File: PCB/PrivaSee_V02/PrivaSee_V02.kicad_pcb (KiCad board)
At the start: 4 copper layers, 73.8 x 90 mm, 32 parts, among them J1 RFPC-SMA27-F, J2 Batt_Solder_Point, J3 Conn_02x06_Odd_Even, J4 VOUT_TEST, J5 GND_TEST, J6 IR_TEST, J7 RF_TEST, SW1 Switch, SW2 SW_Push, U2 LM358, U3 254, U4 DFR0568, U6 ESP32-C5-DevKitC-1

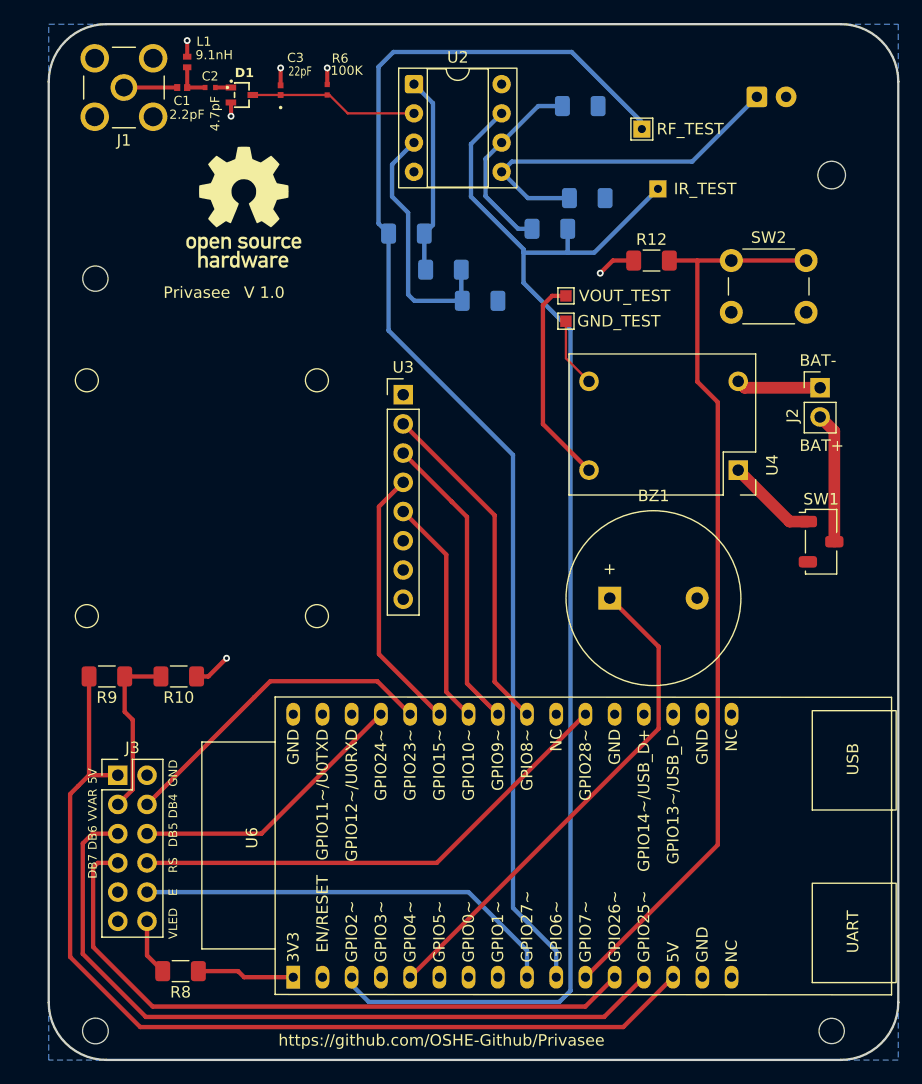
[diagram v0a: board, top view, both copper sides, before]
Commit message: Schematic + RF Fixes
Also changed button position
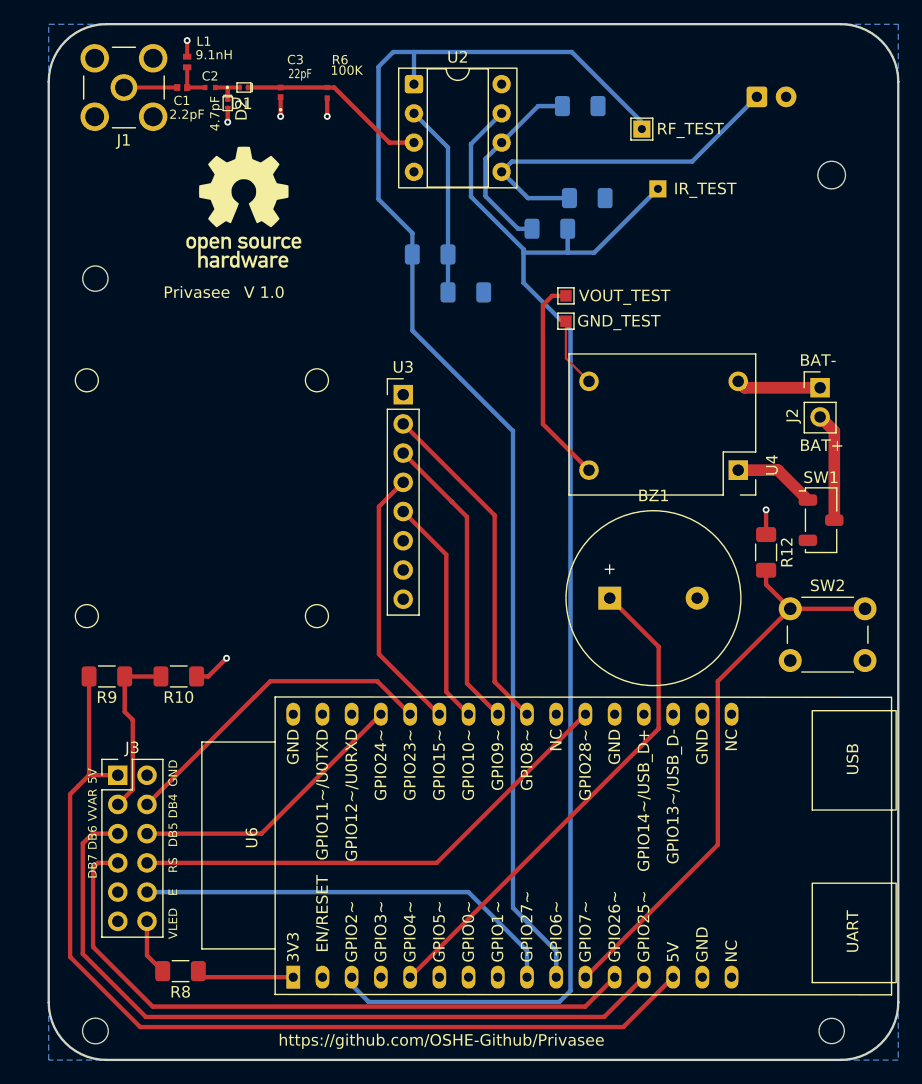
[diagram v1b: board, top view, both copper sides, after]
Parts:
- removed R2: 470 Ohm, Resistor_SMD:R_1206_3216Metric_Pad1.30x1.75mm_HandSolder
- added D2: BAT_15-02EL_E6327, JLCImport:BAT_15-02EL_E6327, F.Cu at (81.6, 28.5)
- D1: value BAT1504WH6327XTSA1 -> BAT_15-02EL_E6327; footprint JLCImport:BAT1504WH6327XTSA1 -> JLCImport:BAT_15-02EL_E6327
- moved SW2 30.7 mm to (130.5, 72.4)
- moved R12 27.3 mm to (128.4, 67.5), turned to -90 degrees
- moved SW1 1.87 mm to (133.2, 64.7)
- moved R1 1.76 mm to (99.2, 41.6), turned to 0 degrees
- moved R7 1.44 mm to (102.3, 44.9)
- moved D1 0.67 mm to (83.0, 27.1)
- moved R6 0.26 mm to (90.2, 27.5)
- moved C3 0.19 mm to (86.2, 27.5)
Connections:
- C3 pad 1: Net-(D1-C/A) -> GND
- C3 pad 2: GND -> Net-(D1-C)
- D1 pad 1: Net-(D1-A) -> Net-(D1-C)
- D1 pad 2: GND -> Net-(D1-A)
- R1 pad 1: Net-(U2A-+) -> Net-(J7-Pin_1)
- R1 pad 2: Net-(R1-Pad2) -> Net-(U2A--)
- R6 pad 1: GND -> Net-(D1-C)
- R6 pad 2: Net-(D1-C/A) -> GND
- R7 pad 1: Net-(U2A-+) -> Net-(U2A--)
- U2 pad 1: Net-(R1-Pad2) -> Net-(J7-Pin_1)
- U2 pad 2: Net-(D1-C/A) -> Net-(U2A--)
- U2 pad 3: Net-(U2A-+) -> Net-(D1-C)
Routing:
- net Net-(U6-GPIO7): track 79.7 -> 50.1 mm
- net Net-(U2A-+): track 22.1 -> 0.00 mm
- net Net-(R1-Pad2): track 17.2 -> 0.00 mm
- net Net-(U2A--): track 0.00 -> 17.1 mm
- net Net-(D1-C): track 0.00 -> 16.4 mm
- net Net-(D1-C/A): track 15.0 -> 0.00 mm
- net Net-(J7-Pin_1): track 112.5 -> 115.3 mm
- net Net-(D1-A): track 1.35 -> 3.22 mm
- net /BAT+: track 11.4 -> 9.48 mm
- net GND: track 18.3 -> 17.5 mm
- net Net-(SW1-C): track 7.91 -> 7.13 mm
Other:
- board text removed: "D1"

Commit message: potentiometer addition
Included a pot for variable gain instead of set amount
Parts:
- added R11: 3310Y-001-103L, Snapeda:TRIM_3310Y-001-103L, F.Cu at (104.5, 52.7)
- R1: value 200 -> 100
- R7: value 10 -> 100
- moved ? 6.00 mm to (77.0, 37.5)
- moved R7 2.20 mm to (103.4, 43.0)
- moved R1 1.70 mm to (99.2, 39.9)
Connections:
- R1 pad 1: Net-(J7-Pin_1) -> Net-(R1-Pad1)
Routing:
- net Net-(R1-Pad1): track 0.00 -> 15.4 mm
- net Net-(U2A--): track 17.1 -> 15.7 mm
- net Net-(J7-Pin_1): track 115.3 -> 116.0 mm

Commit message: trace changes
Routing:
- net GND: track 17.5 -> 15.0 mm
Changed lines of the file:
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@@
 		(start 80.527284 27.0882)
 		(end 81.6 27.0882)
-		(width 0.355476)
+		(width 0.5)
 		(layer "F.Cu")
 		(net "Net-(D1-A)")
@@
 		(start 81.6 28.17)
 		(end 81.6 27.0882)
-		(width 0.381)
+		(width 0.5)
 		(layer "F.Cu")
 		(net "Net-(D1-A)")
@@
 		(start 81.6 27.0882)
 		(end 82.67 27.0882)
-		(width 0.355476)
+		(width 0.5)
 		(layer "F.Cu")
 		(net "Net-(D1-A)")
 	)
 	(segment
-		(start 78.075 27.0882)
-		(end 78.075 25.33)
-		(width 0.355476)
+		(start 78.075 25.33)
+		(end 78.075 27.0882)
+		(width 0.5)
 		(layer "F.Cu")
 		(net "Net-(C1-Pad1)")
 	)
 	(segment
-		(start 78.075 27.0882)
-		(end 79.638284 27.0882)
-		(width 0.355476)
+		(start 79.638284 27.0882)
+		(end 78.075 27.0882)
+		(width 0.5)
 		(layer "F.Cu")
 		(net "Net-(C1-Pad1)")
@@
 	)
 	(segment
-		(start 90.25 29.6)
-		(end 90.25 28.0026)
-		(width 0.381)
+		(start 78.075 23.6)
+		(end 78.075 24.41)
+		(width 0.5)
 		(layer "F.Cu")
 		(net "GND")
@@
 	)
 	(segment
+		(start 81.6 29.6)
+		(end 81.6 28.845)
+		(width 0.45)
+		(layer "F.Cu")
+		(net "GND")
+	)
+	(segment
 		(start 78.08 24.4)
 		(end 78.07 24.41)
 		(width 0.2)
+		(layer "F.Cu")
+		(net "GND")
+	)
+	(segment
+		(start 90.25 28.9)
+		(end 90.25 28.0026)
+		(width 0.381)
+		(layer "F.Cu")
+		(net "GND")
+	)
+	(segment
+		(start 86.2 28.9)
+		(end 86.2 27.9264)
+		(width 0.381)
 		(layer "F.Cu")
 		(net "GND")
@@
 		(net "GND")
 	)
-	(segment
-		(start 81.6 30.1)
-		(end 81.6 28.83)
-		(width 0.381)
-		(layer "F.Cu")
-		(net "GND")
-	)
-	(segment
-		(start 86.2 29.6)
-		(end 86.2 27.9264)
-		(width 0.381)
-		(layer "F.Cu")
-		(net "GND")
-	)
-	(segment
-		(start 78.075 23.01)
-		(end 78.075 24.4)
-		(width 0.355476)
-		(layer "F.Cu")
-		(net "GND")
-	)
 	(via
-		(at 81.6 30.1)
+		(at 81.6 29.6)
 		(size 0.6)
 		(drill 0.3)
@@
 	)
 	(via
-		(at 90.25 29.6)
+		(at 90.25 28.9)
 		(size 0.6)
 		(drill 0.3)
@@
 	)
 	(via
-		(at 86.2 29.6)
+		(at 86.2 28.9)
 		(size 0.6)
 		(drill 0.3)
@@
 	)
 	(via
-		(at 78.075 23.01)
+		(at 78.075 23.6)
 		(size 0.6)
 		(drill 0.3)

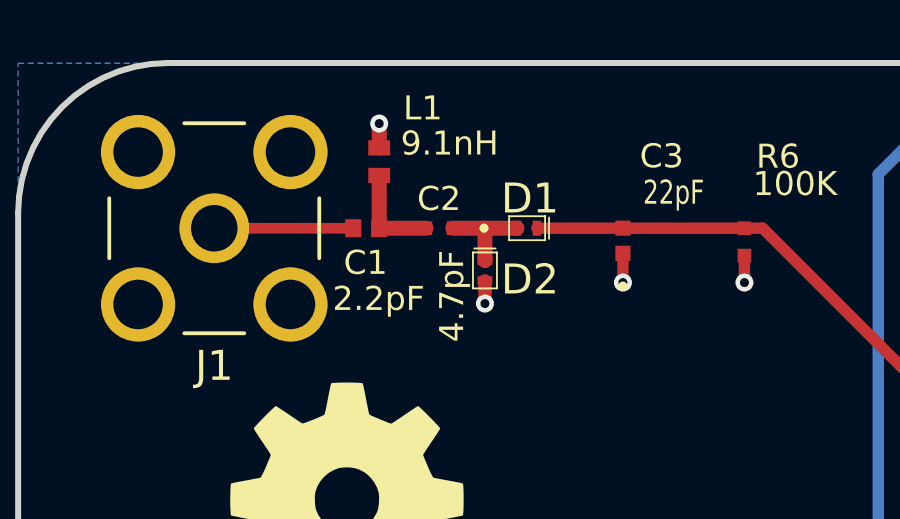
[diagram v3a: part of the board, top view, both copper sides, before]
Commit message: trace adjustments
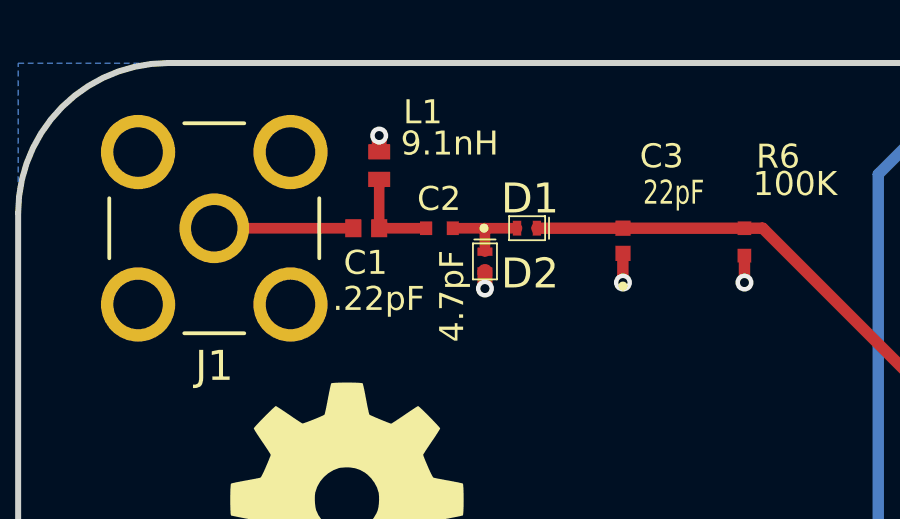
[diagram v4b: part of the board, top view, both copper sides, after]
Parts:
- moved D2 0.30 mm to (81.6, 28.2)
- moved L1 0.13 mm to (78.1, 25.0)
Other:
- board text added: ".22pF"
- board text removed: "2.2pF"
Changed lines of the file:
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@@
 	(footprint "Snapeda:INDC1006X60N"
 		(layer "F.Cu")
-		(at 78.075 24.87 -90)
+		(at 78.075 25 -90)
 		(property "Reference" "L1"
 			(at -1.78 -1.455 0)
@@
 	(footprint "JLCImport:BAT_15-02EL_E6327"
 		(layer "F.Cu")
-		(at 81.6 28.5 -90)
+		(at 81.6 28.2 -90)
 		(descr "1 Independent 110mA 350mV@10mA 4V 5uA@1V TSLP-2 Schottky Diodes ROHS")
 		(tags "BAT1502ELE6327 C533619 Infineon Technologies TSLP-2-19_L1.0-W0.6-P0.65-RD")
 		(property "Reference" "D2"
-			(at 0.3 -1.5 180)
+			(at 0.4 -1.5 180)
 			(layer "F.SilkS")
 			(effects
@@
 		)
 	)
-	(gr_text "2.2pF"
+	(gr_text ".22pF"
 		(at 76.52 29.91 0)
 		(layer "F.SilkS")
@@
 	)
 	(segment
-		(start 80.527284 27.0882)
+		(start 81.6 27.87)
 		(end 81.6 27.0882)
-		(width 0.5)
+		(width 0.355476)
 		(layer "F.Cu")
 		(net "Net-(D1-A)")
 	)
 	(segment
-		(start 81.6 28.17)
+		(start 80.527284 27.0882)
 		(end 81.6 27.0882)
-		(width 0.5)
+		(width 0.355476)
 		(layer "F.Cu")
 		(net "Net-(D1-A)")
@@
 		(start 81.6 27.0882)
 		(end 82.67 27.0882)
-		(width 0.5)
+		(width 0.355476)
 		(layer "F.Cu")
 		(net "Net-(D1-A)")
 	)
 	(segment
-		(start 78.075 25.33)
+		(start 78.075 25.46)
 		(end 78.075 27.0882)
-		(width 0.5)
+		(width 0.355476)
 		(layer "F.Cu")
 		(net "Net-(C1-Pad1)")
 	)
 	(segment
-		(start 79.638284 27.0882)
-		(end 78.075 27.0882)
-		(width 0.5)
+		(start 78.075 27.0882)
+		(end 79.638284 27.0882)
+		(width 0.355476)
 		(layer "F.Cu")
 		(net "Net-(C1-Pad1)")
@@
 	)
 	(segment
-		(start 78.075 23.6)
-		(end 78.075 24.41)
-		(width 0.5)
-		(layer "F.Cu")
-		(net "GND")
-	)
-	(segment
 		(start 111 50.625)
 		(end 111 47.3)
@@
 	)
 	(segment
+		(start 78.075 24)
+		(end 78.075 24.54)
+		(width 0.5)
+		(layer "F.Cu")
+		(net "GND")
+	)
+	(segment
 		(start 81.5 76.7)
 		(end 79.9172 78.2828)
@@
 	)
 	(segment
-		(start 81.6 29.6)
-		(end 81.6 28.845)
-		(width 0.45)
-		(layer "F.Cu")
-		(net "GND")
-	)
-	(segment
-		(start 78.08 24.4)
-		(end 78.07 24.41)
-		(width 0.2)
-		(layer "F.Cu")
-		(net "GND")
-	)
-	(segment
 		(start 90.25 28.9)
 		(end 90.25 28.0026)
@@
 		(net "GND")
 	)
+	(segment
+		(start 81.6 29.1)
+		(end 81.6 28.53)
+		(width 0.5)
+		(layer "F.Cu")
+		(net "GND")
+	)
 	(via
-		(at 81.6 29.6)
+		(at 81.6 29.1)
 		(size 0.6)
 		(drill 0.3)
@@
 	)
 	(via
-		(at 78.075 23.6)
+		(at 78.075 24)
 		(size 0.6)
 		(drill 0.3)

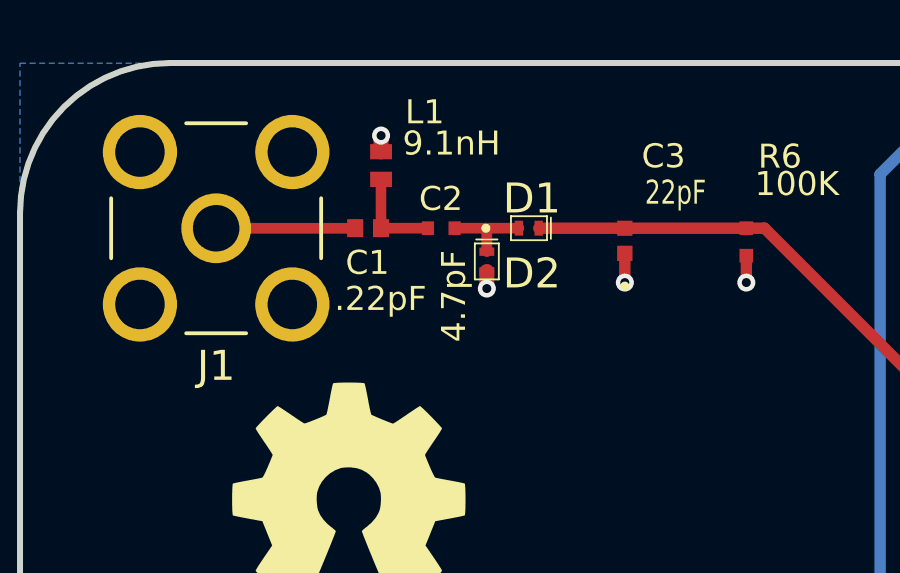
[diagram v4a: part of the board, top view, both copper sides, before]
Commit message: added taper to c2, d1, d2 junction
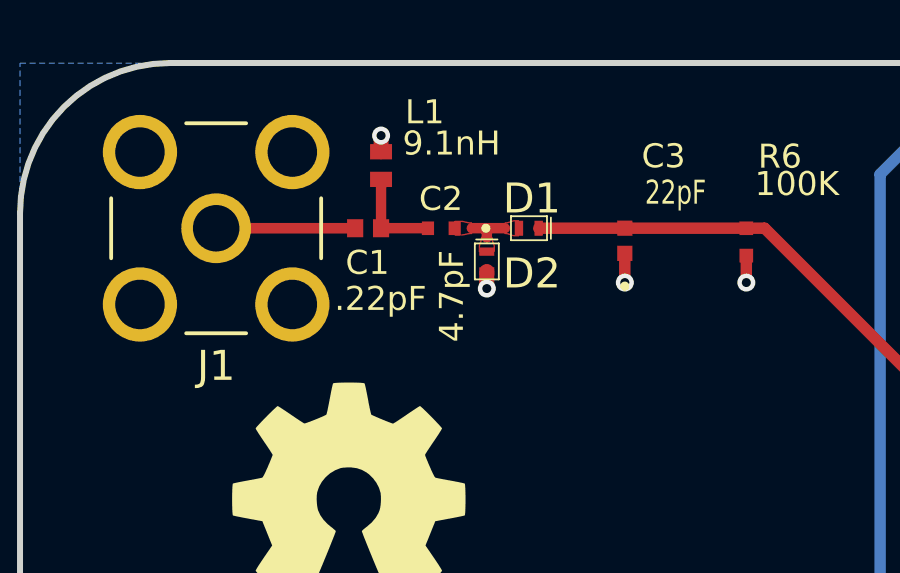
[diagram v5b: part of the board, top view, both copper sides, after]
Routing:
- net Net-(D1-A): track 2.92 -> 1.41 mm
- added copper zone on F.Cu, net Net-(D1-A)
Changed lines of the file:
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@@
 		)
 		(fp_text user "${REFERENCE}"
-			(at -0.107216 -1.8518 0)
+			(at 0 0 0)
 			(unlocked yes)
 			(layer "F.Fab")
@@
 	)
 	(gr_text "4.7pF"
-		(at 80.97 30.89 90)
+		(at 80.9 30.89 90)
 		(layer "F.SilkS")
 		(effects
@@
 	)
 	(segment
-		(start 81.6 27.87)
+		(start 81.6 27.4)
 		(end 81.6 27.0882)
-		(width 0.355476)
+		(width 0.35)
 		(layer "F.Cu")
 		(net "Net-(D1-A)")
 	)
 	(segment
-		(start 80.527284 27.0882)
+		(start 81.1 27.0882)
 		(end 81.6 27.0882)
-		(width 0.355476)
+		(width 0.35)
 		(layer "F.Cu")
 		(net "Net-(D1-A)")
@@
 	(segment
 		(start 81.6 27.0882)
-		(end 82.67 27.0882)
-		(width 0.355476)
+		(end 82.2 27.0882)
+		(width 0.35)
 		(layer "F.Cu")
 		(net "Net-(D1-A)")
 	)
 	(segment
-		(start 78.075 25.46)
-		(end 78.075 27.0882)
-		(width 0.355476)
+		(start 78.075 27.0882)
+		(end 78.075 25.46)
+		(width 0.35)
 		(layer "F.Cu")
 		(net "Net-(C1-Pad1)")
@@
 		(start 78.075 27.0882)
 		(end 79.638284 27.0882)
-		(width 0.355476)
+		(width 0.35)
 		(layer "F.Cu")
 		(net "Net-(C1-Pad1)")
@@
 	)
 	(zone
+		(net "Net-(D1-A)")
+		(layer "F.Cu")
+		(hatch edge 0.5)
+		(priority 17540)
+		(connect_pads yes
+			(clearance 0)
+		)
+		(min_thickness 0.0254)
+		(fill yes
+			(thermal_gap 0.5)
+			(thermal_bridge_width 0.5)
+			(island_removal_mode 0)
+		)
+		(polygon
+			(pts
+				(xy 81.6 27.37375) (xy 81.425 27.3972) (xy 81.4229 27.444513) (xy 81.4172 27.48503) (xy 81.408799 27.520128)
+				(xy 81.3986 27.551189) (xy 81.3875 27.579591) (xy 81.3764 27.606713) (xy 81.3662 27.633936) (xy 81.3578 27.662638)
+				(xy 81.3521 27.6942) (xy 81.35 27.73) (xy 81.35 27.87) (xy 81.6 27.9) (xy 81.85 27.87) (xy 81.85 27.73)
+				(xy 81.8479 27.6942) (xy 81.8422 27.662638) (xy 81.833799 27.633936) (xy 81.8236 27.606713) (xy 81.8125 27.579591)
+				(xy 81.8014 27.551189) (xy 81.7912 27.520128) (xy 81.7828 27.48503) (xy 81.7771 27.444513) (xy 81.775 27.3972)
+			)
+		)
+	)
+	(zone
+		(net "Net-(D1-A)")
+		(layer "F.Cu")
+		(hatch edge 0.5)
+		(priority 17540)
+		(connect_pads yes
+			(clearance 0)
+		)
+		(min_thickness 0.0254)
+		(fill yes
+			(thermal_gap 0.5)
+			(thermal_bridge_width 0.5)
+			(island_removal_mode 0)
+		)
+		(polygon
+			(pts
+				(xy 82.17375 27.0882) (xy 82.1972 27.2632) (xy 82.244513 27.2653) (xy 82.28503 27.271) (xy 82.320128 27.279399)
+				(xy 82.351189 27.2896) (xy 82.379591 27.3007) (xy 82.406713 27.3118) (xy 82.433936 27.321999) (xy 82.462638 27.3304)
+				(xy 82.4942 27.3361) (xy 82.53 27.3382) (xy 82.67 27.3382) (xy 82.7 27.0882) (xy 82.67 26.8382)
+				(xy 82.53 26.8382) (xy 82.4942 26.8403) (xy 82.462638 26.846) (xy 82.433936 26.854399) (xy 82.406713 26.8646)
+				(xy 82.379591 26.8757) (xy 82.351189 26.8868) (xy 82.320128 26.896999) (xy 82.28503 26.9054) (xy 82.244513 26.9111)
+				(xy 82.1972 26.9132)
+			)
+		)
+	)
+	(zone
+		(net "Net-(D1-A)")
+		(layer "F.Cu")
+		(hatch edge 0.5)
+		(priority 17540)
+		(connect_pads yes
+			(clearance 0)
+		)
+		(min_thickness 0.0254)
+		(fill yes
+			(thermal_gap 0.5)
+			(thermal_bridge_width 0.5)
+			(island_removal_mode 0)
+		)
+		(polygon
+			(pts
+				(xy 81.12625 27.0882) (xy 81.104064 26.9132) (xy 81.05157 26.911699) (xy 81.006336 26.907625) (xy 80.966901 26.901622)
+				(xy 80.931804 26.894332) (xy 80.899583 26.8864) (xy 80.868777 26.878467) (xy 80.837925 26.871177)
+				(xy 80.805567 26.865174) (xy 80.77024 26.8611) (xy 80.730484 26.8596) (xy 80.527284 26.8596) (xy 80.499852 27.0882)
+				(xy 80.527284 27.3168) (xy 80.730484 27.3168) (xy 80.77024 27.315299) (xy 80.805567 27.311225) (xy 80.837925 27.305222)
+				(xy 80.868777 27.297932) (xy 80.899583 27.29) (xy 80.931804 27.282067) (xy 80.966901 27.274777)
+				(xy 81.006336 27.268774) (xy 81.05157 27.2647) (xy 81.104064 27.2632)
+			)
+		)
+	)
+	(zone

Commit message: more trace changes
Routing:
- net Net-(D1-A): track 1.41 -> 2.88 mm
- removed copper zone on F.Cu, net Net-(D1-A)
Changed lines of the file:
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@@
 	)
 	(segment
-		(start 81.6 27.4)
+		(start 81.6 27.0882)
+		(end 82.67 27.0882)
+		(width 0.5)
+		(layer "F.Cu")
+		(net "Net-(D1-A)")
+	)
+	(segment
+		(start 81.6 27.0882)
+		(end 81.6 27.83)
+		(width 0.5)
+		(layer "F.Cu")
+		(net "Net-(D1-A)")
+	)
+	(segment
+		(start 80.527284 27.0882)
 		(end 81.6 27.0882)
-		(width 0.35)
-		(layer "F.Cu")
-		(net "Net-(D1-A)")
-	)
-	(segment
-		(start 81.1 27.0882)
-		(end 81.6 27.0882)
-		(width 0.35)
-		(layer "F.Cu")
-		(net "Net-(D1-A)")
-	)
-	(segment
-		(start 81.6 27.0882)
-		(end 82.2 27.0882)
-		(width 0.35)
+		(width 0.5)
 		(layer "F.Cu")
 		(net "Net-(D1-A)")
@@
 		(start 81.6 29.1)
 		(end 81.6 28.53)
-		(width 0.5)
+		(width 0.45)
 		(layer "F.Cu")
 		(net "GND")
@@
 	)
 	(zone
-		(net "Net-(D1-A)")
-		(layer "F.Cu")
-		(hatch edge 0.5)
-		(priority 17540)
-		(connect_pads yes
-			(clearance 0)
-		)
-		(min_thickness 0.0254)
-		(fill yes
-			(thermal_gap 0.5)
-			(thermal_bridge_width 0.5)
-			(island_removal_mode 0)
-		)
-		(polygon
-			(pts
-				(xy 81.6 27.37375) (xy 81.425 27.3972) (xy 81.4229 27.444513) (xy 81.4172 27.48503) (xy 81.408799 27.520128)
-				(xy 81.3986 27.551189) (xy 81.3875 27.579591) (xy 81.3764 27.606713) (xy 81.3662 27.633936) (xy 81.3578 27.662638)
-				(xy 81.3521 27.6942) (xy 81.35 27.73) (xy 81.35 27.87) (xy 81.6 27.9) (xy 81.85 27.87) (xy 81.85 27.73)
-				(xy 81.8479 27.6942) (xy 81.8422 27.662638) (xy 81.833799 27.633936) (xy 81.8236 27.606713) (xy 81.8125 27.579591)
-				(xy 81.8014 27.551189) (xy 81.7912 27.520128) (xy 81.7828 27.48503) (xy 81.7771 27.444513) (xy 81.775 27.3972)
-			)
-		)
-	)
-	(zone
-		(net "Net-(D1-A)")
-		(layer "F.Cu")
-		(hatch edge 0.5)
-		(priority 17540)
-		(connect_pads yes
-			(clearance 0)
-		)
-		(min_thickness 0.0254)
-		(fill yes
-			(thermal_gap 0.5)
-			(thermal_bridge_width 0.5)
-			(island_removal_mode 0)
-		)
-		(polygon
-			(pts
-				(xy 82.17375 27.0882) (xy 82.1972 27.2632) (xy 82.244513 27.2653) (xy 82.28503 27.271) (xy 82.320128 27.279399)
-				(xy 82.351189 27.2896) (xy 82.379591 27.3007) (xy 82.406713 27.3118) (xy 82.433936 27.321999) (xy 82.462638 27.3304)
-				(xy 82.4942 27.3361) (xy 82.53 27.3382) (xy 82.67 27.3382) (xy 82.7 27.0882) (xy 82.67 26.8382)
-				(xy 82.53 26.8382) (xy 82.4942 26.8403) (xy 82.462638 26.846) (xy 82.433936 26.854399) (xy 82.406713 26.8646)
-				(xy 82.379591 26.8757) (xy 82.351189 26.8868) (xy 82.320128 26.896999) (xy 82.28503 26.9054) (xy 82.244513 26.9111)
-				(xy 82.1972 26.9132)
-			)
-		)
-	)
-	(zone
-		(net "Net-(D1-A)")
-		(layer "F.Cu")
-		(hatch edge 0.5)
-		(priority 17540)
-		(connect_pads yes
-			(clearance 0)
-		)
-		(min_thickness 0.0254)
-		(fill yes
-			(thermal_gap 0.5)
-			(thermal_bridge_width 0.5)
-			(island_removal_mode 0)
-		)
-		(polygon
-			(pts
-				(xy 81.12625 27.0882) (xy 81.104064 26.9132) (xy 81.05157 26.911699) (xy 81.006336 26.907625) (xy 80.966901 26.901622)
-				(xy 80.931804 26.894332) (xy 80.899583 26.8864) (xy 80.868777 26.878467) (xy 80.837925 26.871177)
-				(xy 80.805567 26.865174) (xy 80.77024 26.8611) (xy 80.730484 26.8596) (xy 80.527284 26.8596) (xy 80.499852 27.0882)
-				(xy 80.527284 27.3168) (xy 80.730484 27.3168) (xy 80.77024 27.315299) (xy 80.805567 27.311225) (xy 80.837925 27.305222)
-				(xy 80.868777 27.297932) (xy 80.899583 27.29) (xy 80.931804 27.282067) (xy 80.966901 27.274777)
-				(xy 81.006336 27.268774) (xy 81.05157 27.2647) (xy 81.104064 27.2632)
-			)
-		)
-	)
-	(zone
